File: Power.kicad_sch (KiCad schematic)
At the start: 14 parts, among them Q100 AO3401A, U100 LM2842X

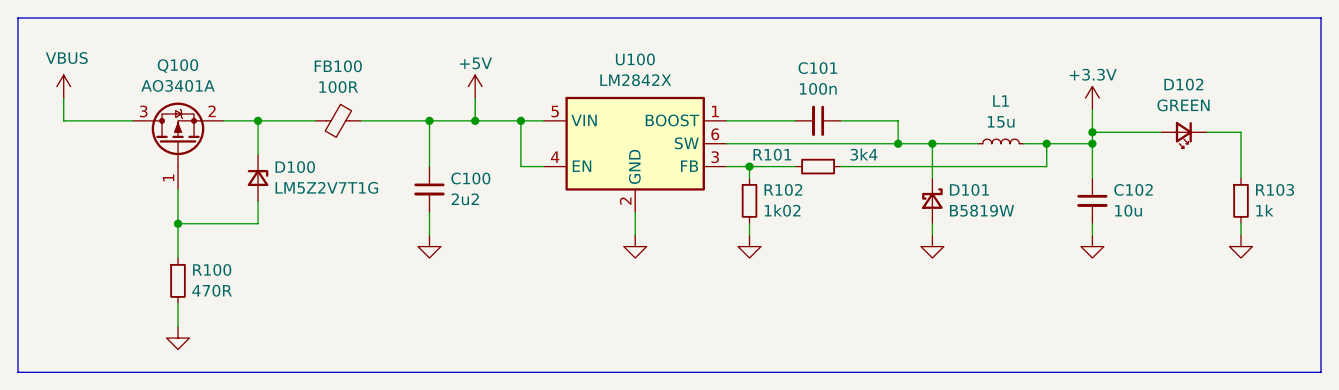
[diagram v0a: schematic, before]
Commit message: gpio breakout stuff
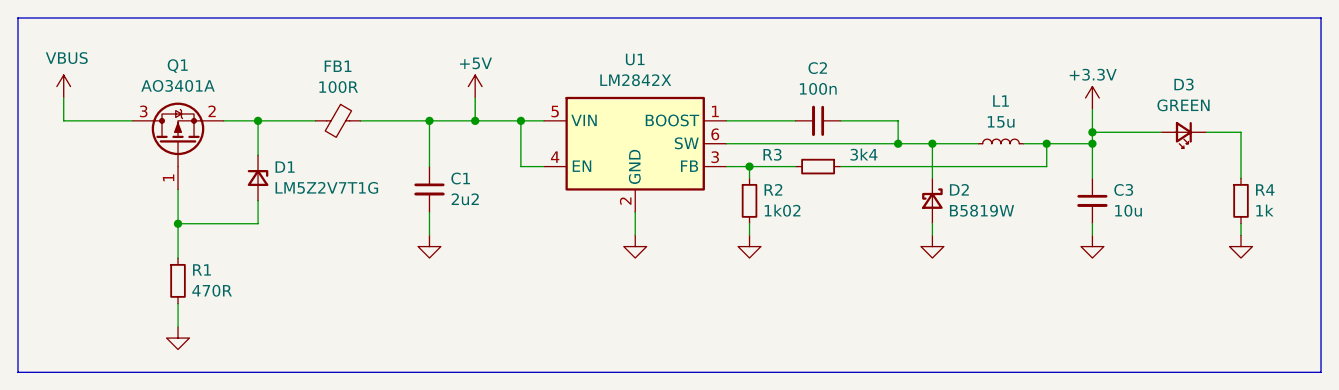
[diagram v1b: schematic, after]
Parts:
- renumbered C100 to C1, C101 to C2, C102 to C3, D100 to D1, D101 to D2, D102 to D3, FB100 to FB1, Q100 to Q1, R100 to R1, R102 to R2, R101 to R3, R103 to R4, U100 to U1
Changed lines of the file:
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@@
   (symbol (lib_id "Transistor_FET:AO3401A") (at 87.63 83.82 90) (unit 1)
     (in_bom yes) (on_board yes)
-    (property "Reference" "Q100" (id 0) (at 87.63 75.1332 90))
+    (property "Reference" "Q1" (id 0) (at 87.63 75.1332 90))
     (property "Value" "AO3401A" (id 1) (at 87.63 77.4446 90))
     (property "Footprint" "Package_TO_SOT_SMD:SOT-23" (id 2) (at 89.535 78.74 0)
@@
   (symbol (lib_id "Device:D_Zener_Small") (at 96.52 87.63 270) (unit 1)
     (in_bom yes) (on_board yes)
-    (property "Reference" "D100" (id 0) (at 98.298 86.4616 90)
+    (property "Reference" "D1" (id 0) (at 98.298 86.4616 90)
       (effects (font (size 1.27 1.27)) (justify left))
     )
@@
   (symbol (lib_id "Device:R_Small") (at 87.63 99.06 0) (unit 1)
     (in_bom yes) (on_board yes)
-    (property "Reference" "R100" (id 0) (at 89.1286 97.8916 0)
+    (property "Reference" "R1" (id 0) (at 89.1286 97.8916 0)
       (effects (font (size 1.27 1.27)) (justify left))
     )
@@
   (symbol (lib_id "power:GND") (at 87.63 104.14 0) (unit 1)
     (in_bom yes) (on_board yes)
-    (property "Reference" "#PWR070" (id 0) (at 87.63 110.49 0)
+    (property "Reference" "#PWR02" (id 0) (at 87.63 110.49 0)
       (effects (font (size 1.27 1.27)) hide)
     )
@@
   (symbol (lib_id "BluePhil-rescue:Ferrite_Bead_Small-Device") (at 105.41 81.28 270) (unit 1)
     (in_bom yes) (on_board yes)
-    (property "Reference" "FB100" (id 0) (at 105.41 75.2602 90))
+    (property "Reference" "FB1" (id 0) (at 105.41 75.2602 90))
     (property "Value" "100R" (id 1) (at 105.41 77.5716 90))
     (property "Footprint" "Inductor_SMD:L_0603_1608Metric" (id 2) (at 105.41 79.502 90)
@@
   (symbol (lib_id "power:VBUS") (at 74.93 78.74 0) (unit 1)
     (in_bom yes) (on_board yes)
-    (property "Reference" "#PWR062" (id 0) (at 74.93 82.55 0)
+    (property "Reference" "#PWR01" (id 0) (at 74.93 82.55 0)
       (effects (font (size 1.27 1.27)) hide)
     )
@@
   (symbol (lib_id "Regulator_Switching:LM2842X") (at 138.43 83.82 0) (unit 1)
     (in_bom yes) (on_board yes)
-    (property "Reference" "U100" (id 0) (at 138.43 74.4982 0))
+    (property "Reference" "U1" (id 0) (at 138.43 74.4982 0))
     (property "Value" "LM2842X" (id 1) (at 138.43 76.8096 0))
     (property "Footprint" "Package_TO_SOT_SMD:TSOT-23-6" (id 2) (at 139.065 90.17 0)
@@
   (symbol (lib_id "Device:C_Small") (at 115.57 88.9 0) (unit 1)
     (in_bom yes) (on_board yes)
-    (property "Reference" "C100" (id 0) (at 117.9068 87.7316 0)
+    (property "Reference" "C1" (id 0) (at 117.9068 87.7316 0)
       (effects (font (size 1.27 1.27)) (justify left))
     )
@@
   (symbol (lib_id "power:GND") (at 115.57 93.98 0) (unit 1)
     (in_bom yes) (on_board yes)
-    (property "Reference" "#PWR064" (id 0) (at 115.57 100.33 0)
+    (property "Reference" "#PWR03" (id 0) (at 115.57 100.33 0)
       (effects (font (size 1.27 1.27)) hide)
     )
@@
   (symbol (lib_id "power:GND") (at 138.43 93.98 0) (unit 1)
     (in_bom yes) (on_board yes)
-    (property "Reference" "#PWR065" (id 0) (at 138.43 100.33 0)
+    (property "Reference" "#PWR05" (id 0) (at 138.43 100.33 0)
       (effects (font (size 1.27 1.27)) hide)
     )
@@
   (symbol (lib_id "Device:R_Small") (at 158.75 86.36 270) (unit 1)
     (in_bom yes) (on_board yes)
-    (property "Reference" "R101" (id 0) (at 153.67 85.09 90))
+    (property "Reference" "R3" (id 0) (at 153.67 85.09 90))
     (property "Value" "3k4" (id 1) (at 163.83 85.09 90))
     (property "Footprint" "Resistor_SMD:R_0402_1005Metric" (id 2) (at 158.75 86.36 0)
@@
   (symbol (lib_id "Device:R_Small") (at 151.13 90.17 0) (unit 1)
     (in_bom yes) (on_board yes)
-    (property "Reference" "R102" (id 0) (at 152.6286 89.0016 0)
+    (property "Reference" "R2" (id 0) (at 152.6286 89.0016 0)
       (effects (font (size 1.27 1.27)) (justify left))
     )
@@
   (symbol (lib_id "power:GND") (at 151.13 93.98 0) (unit 1)
     (in_bom yes) (on_board yes)
-    (property "Reference" "#PWR066" (id 0) (at 151.13 100.33 0)
+    (property "Reference" "#PWR06" (id 0) (at 151.13 100.33 0)
       (effects (font (size 1.27 1.27)) hide)
     )
@@
   (symbol (lib_id "Device:D_Schottky_Small") (at 171.45 90.17 270) (unit 1)
     (in_bom yes) (on_board yes)
-    (property "Reference" "D101" (id 0) (at 173.228 89.0016 90)
+    (property "Reference" "D2" (id 0) (at 173.228 89.0016 90)
       (effects (font (size 1.27 1.27)) (justify left))
     )
@@
   (symbol (lib_id "power:GND") (at 171.45 93.98 0) (unit 1)
     (in_bom yes) (on_board yes)
-    (property "Reference" "#PWR067" (id 0) (at 171.45 100.33 0)
+    (property "Reference" "#PWR07" (id 0) (at 171.45 100.33 0)
       (effects (font (size 1.27 1.27)) hide)
     )
@@
   (symbol (lib_id "Device:C_Small") (at 158.75 81.28 270) (unit 1)
     (in_bom yes) (on_board yes)
-    (property "Reference" "C101" (id 0) (at 158.75 75.4634 90))
+    (property "Reference" "C2" (id 0) (at 158.75 75.4634 90))
     (property "Value" "100n" (id 1) (at 158.75 77.7748 90))
     (property "Footprint" "Capacitor_SMD:C_0402_1005Metric" (id 2) (at 158.75 81.28 0)
@@
   (symbol (lib_id "Device:C_Small") (at 189.23 90.17 0) (unit 1)
     (in_bom yes) (on_board yes)
-    (property "Reference" "C102" (id 0) (at 191.5668 89.0016 0)
+    (property "Reference" "C3" (id 0) (at 191.5668 89.0016 0)
       (effects (font (size 1.27 1.27)) (justify left))
     )
@@
   (symbol (lib_id "power:GND") (at 189.23 93.98 0) (unit 1)
     (in_bom yes) (on_board yes)
-    (property "Reference" "#PWR068" (id 0) (at 189.23 100.33 0)
+    (property "Reference" "#PWR09" (id 0) (at 189.23 100.33 0)
       (effects (font (size 1.27 1.27)) hide)
     )
@@
   (symbol (lib_id "BluePhil-rescue:+3.3V-power") (at 189.23 80.01 0) (unit 1)
     (in_bom yes) (on_board yes)
-    (property "Reference" "#PWR063" (id 0) (at 189.23 83.82 0)
+    (property "Reference" "#PWR08" (id 0) (at 189.23 83.82 0)
       (effects (font (size 1.27 1.27)) hide)
     )
@@
   (symbol (lib_id "Device:LED_Small") (at 199.39 82.55 180) (unit 1)
     (in_bom yes) (on_board yes)
-    (property "Reference" "D102" (id 0) (at 199.39 77.2922 0))
+    (property "Reference" "D3" (id 0) (at 199.39 77.2922 0))
     (property "Value" "GREEN" (id 1) (at 199.39 79.6036 0))
     (property "Footprint" "LED_SMD:LED_0603_1608Metric" (id 2) (at 199.39 82.55 90)
@@
   (symbol (lib_id "Device:R_Small") (at 205.74 90.17 0) (unit 1)
     (in_bom yes) (on_board yes)
-    (property "Reference" "R103" (id 0) (at 207.2386 89.0016 0)
+    (property "Reference" "R4" (id 0) (at 207.2386 89.0016 0)
       (effects (font (size 1.27 1.27)) (justify left))
     )
@@
   (symbol (lib_id "power:GND") (at 205.74 93.98 0) (unit 1)
     (in_bom yes) (on_board yes)
-    (property "Reference" "#PWR069" (id 0) (at 205.74 100.33 0)
+    (property "Reference" "#PWR010" (id 0) (at 205.74 100.33 0)
       (effects (font (size 1.27 1.27)) hide)
     )
@@
   (symbol (lib_id "power:+5V") (at 120.65 78.74 0) (unit 1)
     (in_bom yes) (on_board yes)
-    (property "Reference" "#PWR0101" (id 0) (at 120.65 82.55 0)
-      (effects (font (size 1.27 1.27)) hide)
-    )
+    (property "Reference" "#PWR04" (id 0) (at 120.65 82.55 0)
+      (effects (font (size 1.27 1.27)) hide)
+    )

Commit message: siobgg:
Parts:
- added IC1, IC2: ADP2301AUJZ-R7, SOT95P280X100-6N, symbol ADP2301AUJZ-R7:ADP2301AUJZ-R7
- added U6: XT30PW-F, Connector_AMASS:AMASS_XT30PW-F_1x02_P2.50mm_Horizontal, symbol XT30PW-F:XT30PW-F
- added U7: XT30PW-M, Connector_AMASS:AMASS_XT30PW-M_1x02_P2.50mm_Horizontal, symbol XT30PW-F:XT30PW-F
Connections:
- new net COMMON_GND: IC1.2 (GND), IC2.2 (GND), U6.P1 (COMMON_GND), U7.P1 (COMMON_GND)
- new net V_SUPPLY: IC1.5 (VIN), IC2.5 (VIN), U6.P2 (V_SUPPLY), U7.P2 (V_SUPPLY)
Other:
- moved on the sheet: C1, C2, C3, D1, D2, D3, FB1, L1, Q1, R1, R2, R3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

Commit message: adsigjningh
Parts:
- added C21: 10u, Capacitor_SMD:C_0402_1005Metric, symbol Device:C_Small
- added C22: 10u 25V, Capacitor_SMD:C_0402_1005Metric, symbol Device:C_Small
- added C23: C1005X5R1E104K050BC, SnapEDA Library:CAPC1005X55N, symbol C1005X5R1E104K050BC:C1005X5R1E104K050BC
- added C24: 0.1u, Capacitor_SMD:C_0402_1005Metric, symbol Device:C_Small
- added D13: D_Schottky, SnapEDA Library:B230A-13-F, symbol Device:D_Schottky
- added J8: Conn_01x02, SnapEDA Library:JST_BM02B-SURS-TF(LF)(SN), symbol Connector_Generic:Conn_01x02
- added L2: 4.7u 2.0A, SnapEDA Library:CDRH5D28RHPNP-4R7NC, symbol Device:L
- added R19: 56k, Resistor_SMD:R_0402_1005Metric, symbol Device:R_Small
- added R20, R22: 10.2k, Resistor_SMD:R_0402_1005Metric, symbol Device:R_Small
- added R21: 31.6k, Resistor_SMD:R_0402_1005Metric, symbol Device:R_Small
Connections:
- net at IC2.1 (BST): now also C23.1
- net at IC2.3 (FB): now also R21.2, R22.1
- net at IC2.4 (EN): now also R19.2, R20.1
- net at IC2.6 (SW): now also C23.2, D13.1 (K), L2.1
- net COMMON_GND renamed Earth
- net Earth: now also C21.1, C22.1, C24.1, D13.2 (A), J8.2 (Pin_2), R20.2, R22.2
- net V_SUPPLY renamed VS
- net VS: now also C21.2, C22.2, R19.1
- new net: C24.2, J8.1 (Pin_1), L2.2, R21.1
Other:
- note added: "DRS-0101"
- note added: "MCU"
- moved on the sheet: C1, C2, C3, D1, D2, D3, FB1, IC1, IC2, L1, Q1, R1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

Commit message: skgnigniogni
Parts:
- added C25, C26: C0603C105K3RACTU, SnapEDA Library:C0603C105K3RACTU, symbol C0603C105K3RACTU:C0603C105K3RACTU
- added U9: LP5907QMFX-3.3Q1, SnapEDA Library:SOT95P280X145-5N, symbol LP5907QMFX-3.3Q1:LP5907QMFX-3.3Q1
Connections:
- net +3V3: now also C26.2, U9.5 (OUT)
- net +5V: now also C25.2, U9.1 (IN), U9.3 (EN)
- net GND: now also C25.1, C26.1, U9.2 (GND)
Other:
- moved on the sheet: C21, C22, C23, C24, D13, IC1, IC2, J8, L2, R19, R20, R21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

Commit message: sgsegwaebdd
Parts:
- J8: footprint SnapEDA Library:JST_BM02B-SURS-TF(LF)(SN) -> (none)
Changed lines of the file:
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@@
     (pin "6")
-  )
-  (symbol (lib_id "Connector_Generic:Conn_01x02") (at 116.84 144.78 0) (unit 1)
-    (in_bom yes) (on_board yes) (fields_autoplaced)
-    (property "Reference" "J8" (id 0) (at 119.38 144.7799 0)
-      (effects (font (size 1.27 1.27)) (justify left))
-    )
-    (property "Value" "Conn_01x02" (id 1) (at 119.38 147.3199 0)
-      (effects (font (size 1.27 1.27)) (justify left))
-    )
-    (property "Footprint" "SnapEDA Library:JST_BM02B-SURS-TF(LF)(SN)" (id 2) (at 116.84 144.78 0)
-      (effects (font (size 1.27 1.27)) hide)
-    )
-    (property "Datasheet" "~" (id 3) (at 116.84 144.78 0)
-      (effects (font (size 1.27 1.27)) hide)
-    )
-    (pin "1")
-    (pin "2")
   )
   (symbol (lib_id "power:Earth") (at 111.76 151.13 0) (unit 1)
@@
       (effects (font (size 1.27 1.27)) hide)
     )
+    (pin "1")
+    (pin "2")
+  )
+  (symbol (lib_id "Connector_Generic:Conn_01x02") (at 116.84 144.78 0) (unit 1)
+    (in_bom yes) (on_board yes) (fields_autoplaced)
+    (property "Reference" "J8" (id 0) (at 119.38 144.7799 0)
+      (effects (font (size 1.27 1.27)) (justify left))
+    )
+    (property "Value" "Conn_01x02" (id 1) (at 119.38 147.3199 0)
+      (effects (font (size 1.27 1.27)) (justify left))
+    )
+    (property "Footprint" "" (id 2) (at 116.84 144.78 0)
+      (effects (font (size 1.27 1.27)) hide)
+    )
+    (property "Datasheet" "~" (id 3) (at 116.84 144.78 0)
+      (effects (font (size 1.27 1.27)) hide)
+    )

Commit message: sdgionbidnb
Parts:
- removed C21: 10u, Capacitor_SMD:C_0402_1005Metric, symbol Device:C_Small
- removed C22: 10u 25V, Capacitor_SMD:C_0402_1005Metric, symbol Device:C_Small
- removed C24: 0.1u, Capacitor_SMD:C_0402_1005Metric, symbol Device:C_Small
- removed J8: Conn_01x02, symbol Connector_Generic:Conn_01x02
- added C21: 0.1u ceramic X5R, SnapEDA Library:CAPC1005X55N, symbol C1005X5R1E104K050BC:C1005X5R1E104K050BC
- added C22, C24, C27, C28: 10u ceramic X5R, SnapEDA Library:CAPC1608X90N, symbol C1608X5R0J106K080AB:C1608X5R0J106K080AB
- added D14: D_Schottky, SnapEDA Library:B230A-13-F, symbol Device:D_Schottky
- added L3: 4.7u 2.0A, SnapEDA Library:CDRH5D28RHPNP-4R7NC, symbol Device:L
- added R23: 56, Resistor_SMD:R_0402_1005Metric, symbol Device:R_Small
- added R24: 6.8, Resistor_SMD:R_0402_1005Metric, symbol Device:R_Small
- added R25: 56k, Resistor_SMD:R_0402_1005Metric, symbol Device:R_Small
- added R26: 10.2k, Resistor_SMD:R_0402_1005Metric, symbol Device:R_Small
- C23: value C1005X5R1E104K050BC -> 0.1u ceramic X5R
- R21: value 31.6k -> 52.3
- R22: value 10.2k -> 10
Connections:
- net +5V: now also L2.2, R21.1, C24.2
- net Earth: now also C22.1, C24.1, C27.1, C28.1, D14.2 (A), R24.2, R26.2
- net VS: now also C22.2, C27.2, R25.1
- net at IC1.1 (BST): now also C21.1
- net at IC1.3 (FB): now also R23.2, R24.1
- net at IC1.4 (EN): now also R25.2, R26.1
- net at IC1.6 (SW): now also C21.2, D14.1 (K), L3.1
- new net Vdrive: C28.2, L3.2, R23.1
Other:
- note added: "5V"
- note added: "7.4V 1.2A"
- note removed: "MCU"
- moved on the sheet: C23, D13, IC1, IC2, L2, R19, R20, R21, R22

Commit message: WEBGIOWEBGIOBWEG
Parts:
- removed C27: 10u ceramic X5R, SnapEDA Library:CAPC1608X90N, symbol C1608X5R0J106K080AB:C1608X5R0J106K080AB
- removed R25: 56k, Resistor_SMD:R_0402_1005Metric, symbol Device:R_Small
- removed R26: 10.2k, Resistor_SMD:R_0402_1005Metric, symbol Device:R_Small
- removed U6: XT30PW-F, Connector_AMASS:AMASS_XT30PW-F_1x02_P2.50mm_Horizontal, symbol XT30PW-F:XT30PW-F
- removed U7: XT30PW-M, Connector_AMASS:AMASS_XT30PW-M_1x02_P2.50mm_Horizontal, symbol XT30PW-F:XT30PW-F
- added C207: 10u ceramic X5R, SnapEDA Library:CAPC1608X90N, symbol C1608X5R0J106K080AB:C1608X5R0J106K080AB
- added D204: GREEN, LED_SMD:LED_0603_1608Metric, symbol Device:LED_Small
- added F201, F202: Resettable Fuse, symbol Device:Fuse
- added J201: AMASS_XT30PW-F, Connector_AMASS:AMASS_XT30PW-F_1x02_P2.50mm_Horizontal, symbol Connector_Generic:Conn_01x02
- added J202: AMASS_XT30PW-M, Connector_AMASS:AMASS_XT30PW-M_1x02_P2.50mm_Horizontal, symbol Connector_Generic:Conn_01x02
- added R205: 56k, Resistor_SMD:R_0402_1005Metric, symbol Device:R_Small
- added R206: 10.2k, Resistor_SMD:R_0402_1005Metric, symbol Device:R_Small
- added R208: 1k, Resistor_SMD:R_0402_1005Metric, symbol Device:R_Small
- C201: renamed from C25; value C0603C105K3RACTU -> 1u ceramic X7R
- C205: renamed from C26; value C0603C105K3RACTU -> 1u ceramic X7R
- D202: renamed from D14; value D_Schottky -> 30V 2A
- D206: renamed from D13; value D_Schottky -> 30V 2A
- L202: renamed from L1; footprint BluePhil-Footprints:MPIT4018-150M-LF -> BluePill-Footprints:MPIT4018-150M-LF
- R201: renamed from R23; value 56 -> 56k
- R202: renamed from R24; value 6.8 -> 6.8k
- R210: renamed from R21; value 52.3 -> 52.3k
- R211: renamed from R22; value 10 -> 10k
- renumbered C21 to C202, C1 to C203, C28 to C204, C2 to C206, C3 to C208, C23 to C209, C24 to C210, C22 to C211, D1 to D201, D2 to D203, D3 to D205, FB1 to FB201, IC1 to IC201, IC2 to IC202, L3 to L201, L2 to L203, Q1 to Q201, R1 to R203, R2 to R204, R3 to R207, R4 to R209, R19 to R212, R20 to R213, U9 to U201, U1 to U202
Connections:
- net Earth is gone; now on net GND: C204.1, C210.1, C211.1, D202.2 (A), D206.2 (A), IC201.2 (GND), IC202.2 (GND), R202.2, R211.2, R213.2
- net +3V3: now also D204.2 (A)
- net GND: now also C207.1, J201.1 (Pin_1), J202.1 (Pin_1), R206.2, R208.2
- net VS: now also F201.1, F202.1, J201.2 (Pin_2), J202.2 (Pin_2); no longer C211.2, IC201.5 (VIN), IC202.5 (VIN), R212.1
- net at IC201.4 (EN): now also R205.2, R206.1
- new net: C211.2, F202.2, IC202.5 (VIN), R212.1
- new net: D204.1 (K), R208.1
- new net: C207.2, F201.2, IC201.5 (VIN), R205.1
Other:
- note added: "5V/3V3 LDO"
- note added: "Supply connectors and regulators"
- note added: "VBUS regulator (is this still needed??)"
- moved on the sheet: C201, C202, C203, C204, C205, C206, C208, C209, C210, C211, D201, D202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

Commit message: final commit before holiday
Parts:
- removed C203: 2u2, Capacitor_SMD:C_0603_1608Metric, symbol Device:C_Small
- removed C206: 100n, Capacitor_SMD:C_0402_1005Metric, symbol Device:C_Small
- removed C208: 10u, Capacitor_SMD:C_0603_1608Metric, symbol Device:C_Small
- removed D201: LM5Z2V7T1G, Diode_SMD:D_SOD-523, symbol Device:D_Zener_Small
- removed D203: B5819W, Diode_SMD:D_SOD-123, symbol Device:D_Schottky_Small
- removed D205: GREEN, LED_SMD:LED_0603_1608Metric, symbol Device:LED_Small
- removed F201, F202: Resettable Fuse, symbol Device:Fuse
- removed FB201: 100R, Inductor_SMD:L_0603_1608Metric, symbol BluePhil-rescue:Ferrite_Bead_Small-Device
- removed L202: 15u, BluePill-Footprints:MPIT4018-150M-LF, symbol Device:L_Small
- removed Q201: AO3401A, Package_TO_SOT_SMD:SOT-23, symbol Transistor_FET:AO3401A
- removed R203: 470R, Resistor_SMD:R_0402_1005Metric, symbol Device:R_Small
- removed R204: 1k02, Resistor_SMD:R_0402_1005Metric, symbol Device:R_Small
- removed R207: 3k4, Resistor_SMD:R_0402_1005Metric, symbol Device:R_Small
- removed R209: 1k, Resistor_SMD:R_0402_1005Metric, symbol Device:R_Small
- removed U202: LM2842X, Package_TO_SOT_SMD:TSOT-23-6, symbol Regulator_Switching:LM2842X
- added F201, F202: 0ZCG0050FF2C, SnapEDA Library:0ZCG0050FF2C, symbol 0ZCG0050FF2C:0ZCG0050FF2C
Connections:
- net VS: now also F201.2, F202.2
- net at C211.2, IC202.5 (VIN), R212.1: now also F202.1
- net at C207.2, IC201.5 (VIN), R205.1: now also F201.1
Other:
- note removed: "VBUS regulator (is this still needed??)"
